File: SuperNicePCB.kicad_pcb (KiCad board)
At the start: 4 copper layers, 75 x 85 mm, 65 parts, among them J1 UART Debug, J2 Boot Opt, SW1 Reset, U1 ESP32-S3-WROOM-1-N8, U2 SY8089AAAC, U3 SGM2048-ADJXTEK8G/TR, U4 ICS-43434_C5656610, U5 AM312, U6 SCD40-D-R1, U7 SHT40-AD1B-R3, U8 HLK-LD6002, U9 DWM3000TR13

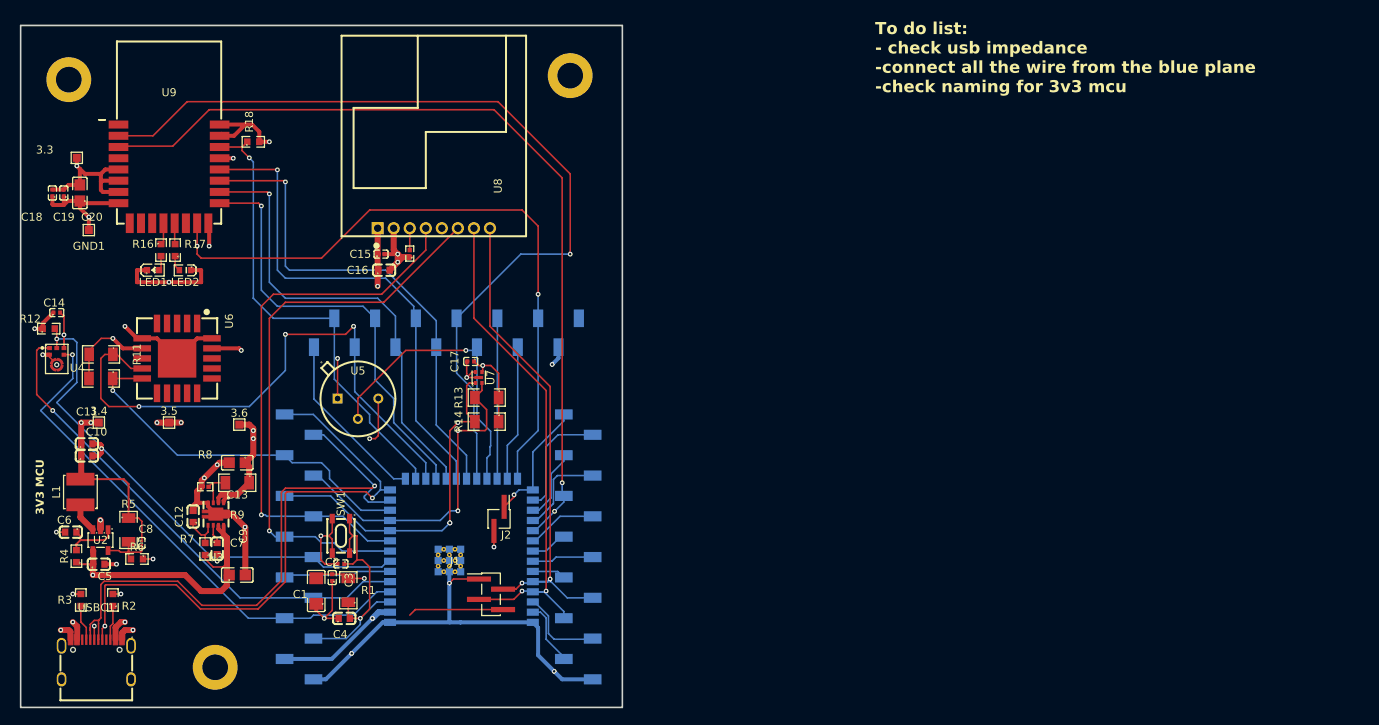
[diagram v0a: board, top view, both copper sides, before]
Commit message: Connect power for uart debug
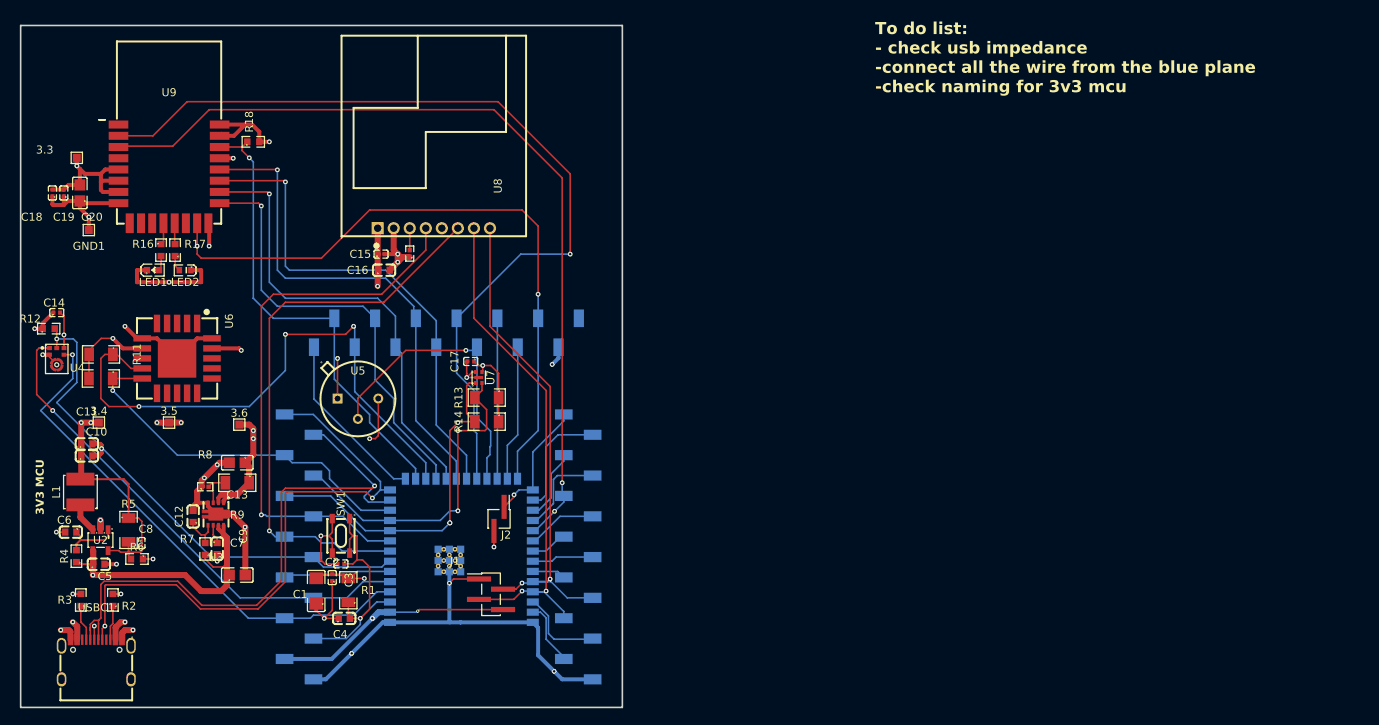
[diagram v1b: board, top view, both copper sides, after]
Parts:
- removed REF** (x3): MountingHole_3.2mm_M3_DIN965_Pad, MountingHole:MountingHole_3.2mm_M3_DIN965_Pad
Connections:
- J1 pad 4: /MCU/VDD33 -> /MCU/3V3_MCU
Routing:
- net /MCU/3V3_MCU: track 115.4 -> 129.7 mm, vias 4 -> 5
- net /MCU/VDD33: track 11.9 -> 0.00 mm

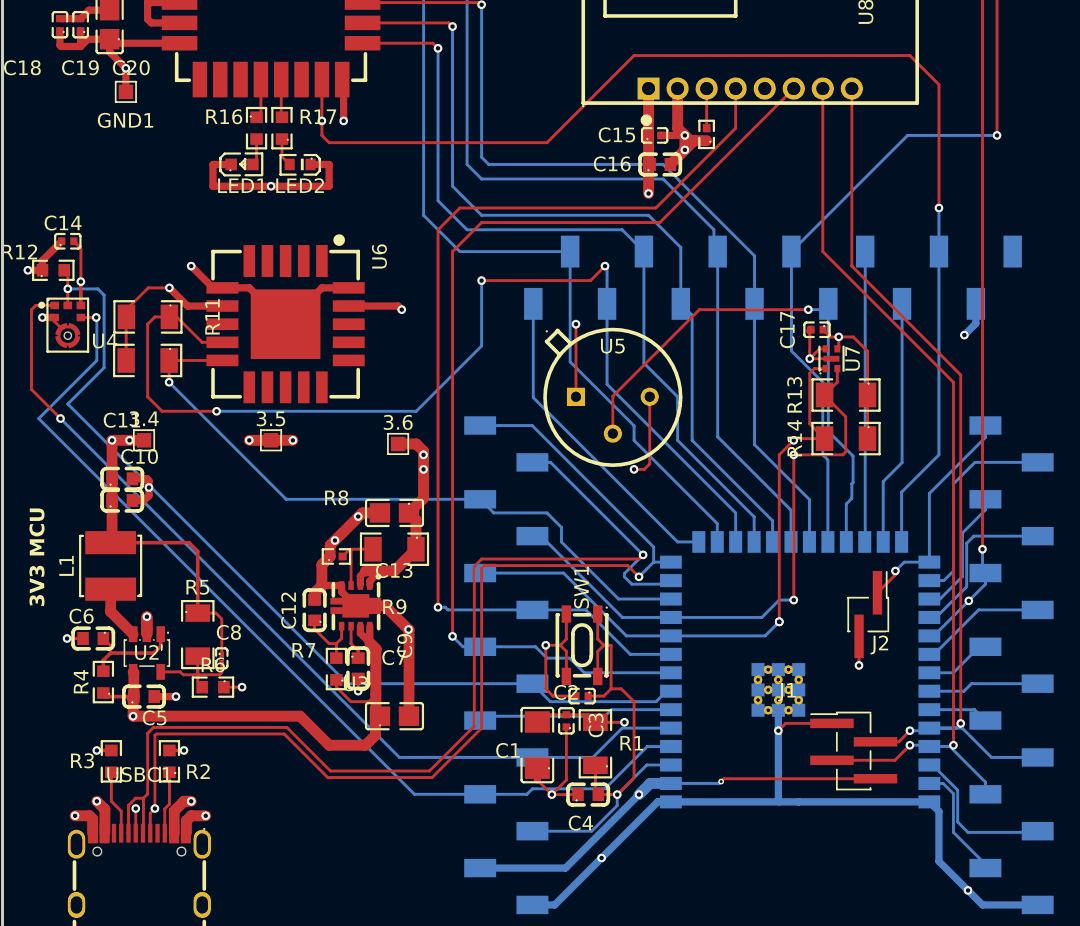
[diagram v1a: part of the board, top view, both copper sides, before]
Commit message: DRC issues resolved
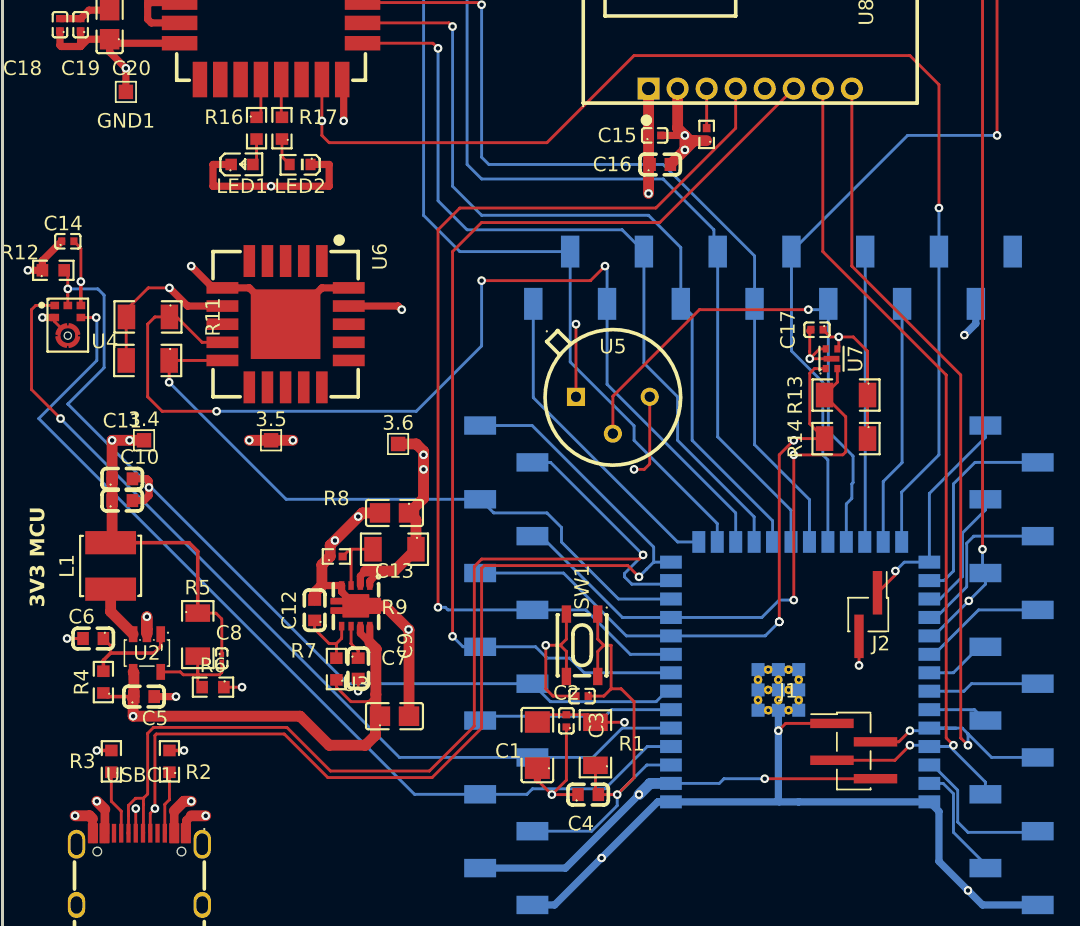
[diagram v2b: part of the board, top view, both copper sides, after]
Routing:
- net /MCU/RXD: track 61.5 -> 63.6 mm
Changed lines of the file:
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@@
 		(at 138.6 110.38 90)
 		(property "Reference" "U7"
-			(at 0 1.48 90)
+			(at 0 1.65 90)
 			(layer "F.SilkS")
 			(effects
@@
 		(at 151 131.49 90)
 		(property "Reference" "H3"
-			(at 0.65 3 90)
+			(at 0.99 2.5 90)
 			(layer "B.SilkS")
 			(effects
@@
 	)
 	(segment
-		(start 131.195 139.305)
-		(end 131 139.5)
-		(width 0.2)
-		(layer "F.Cu")
-		(net "/MCU/3V3_MCU")
-	)
-	(segment
 		(start 89.05 118.65)
 		(end 89.05 122.95)
@@
 	)
 	(segment
-		(start 141.63 139.305)
-		(end 131.195 139.305)
-		(width 0.2)
-		(layer "F.Cu")
-		(net "/MCU/3V3_MCU")
-	)
-	(segment
 		(start 88.95 123.05)
 		(end 94.35 123.05)
@@
 	)
 	(segment
+		(start 134 139.305)
+		(end 141.63 139.305)
+		(width 0.2)
+		(layer "F.Cu")
+		(net "/MCU/3V3_MCU")
+	)
+	(segment
 		(start 96.2 127.9)
 		(end 96.604808 128.304808)
@@
 	)
 	(via
-		(at 131 139.5)
-		(size 0.4)
-		(drill 0.2)
+		(at 134 139.305)
+		(size 0.6)
+		(drill 0.3)
 		(layers "F.Cu" "B.Cu")
 		(net "/MCU/3V3_MCU")
@@
 	)
 	(segment
-		(start 127.54 139.63)
-		(end 130.87 139.63)
-		(width 0.2)
-		(layer "B.Cu")
-		(net "/MCU/3V3_MCU")
-	)
-	(segment
-		(start 130.87 139.63)
-		(end 131 139.5)
-		(width 0.2)
-		(layer "B.Cu")
-		(net "/MCU/3V3_MCU")
-	)
-	(segment
 		(start 125.34 140.4)
 		(end 120.28 145.46)
@@
 	)
 	(segment
+		(start 134 139.305)
+		(end 131.195 139.305)
+		(width 0.2)
+		(layer "B.Cu")
+		(net "/MCU/3V3_MCU")
+	)
+	(segment
 		(start 126.11 139.63)
 		(end 125.34 140.4)
@@
 	)
 	(segment
+		(start 130.87 139.63)
+		(end 127.54 139.63)
+		(width 0.2)
+		(layer "B.Cu")
+		(net "/MCU/3V3_MCU")
+	)
+	(segment
+		(start 131.195 139.305)
+		(end 130.87 139.63)
+		(width 0.2)
+		(layer "B.Cu")
+		(net "/MCU/3V3_MCU")
+	)
+	(segment
 		(start 114 138)
 		(end 114 141.4)
@@
 		(start 87.705102 142.065014)
 		(end 87.705102 143.06)
-		(width 0.75)
+		(width 0.6)
 		(layer "F.Cu")
 		(net "GND")
@@
 	)
 	(segment
+		(start 94.17 142.189912)
+		(end 94.5 141.859912)
+		(width 0.6)
+		(layer "F.Cu")
+		(net "GND")
+	)
+	(segment
 		(start 119.42 133.615)
 		(end 121 133.615)
@@
 	)
 	(segment
-		(start 94.5 141.859912)
-		(end 94.17 142.189912)
-		(width 0.75)
-		(layer "F.Cu")
-		(net "GND")
-	)
-	(segment
 		(start 96.65 105.5)
 		(end 98.5 105.5)
@@
 	)
 	(segment
-		(start 87.5 141.859912)
-		(end 87.705102 142.065014)
-		(width 0.75)
-		(layer "F.Cu")
-		(net "GND")
-	)
-	(segment
 		(start 84.25 103.62)
 		(end 85.58 102.29)
@@
 	)
 	(segment
+		(start 87.5 141.859912)
+		(end 87.705102 142.065014)
+		(width 0.75)
+		(layer "F.Cu")
+		(net "GND")
+	)
+	(segment
 		(start 103 127)
 		(end 103 126.5)
@@
 		(start 94.17 142.189912)
 		(end 94.17 143.06)
-		(width 0.75)
+		(width 0.6)
 		(layer "F.Cu")
 		(net "GND")
@@
 	)
 	(segment
-		(start 140 91.7725)
+		(start 147.5 111.5)
 		(end 140 104)
 		(width 0.2)
@@
 	)
 	(segment
-		(start 147.5 111.5)
-		(end 147.5 135.5)
+		(start 143.235 136.765)
+		(end 144 136)
 		(width 0.2)
 		(layer "F.Cu")
@@
 	)
 	(segment
-		(start 143.235 136.765)
-		(end 144 136)
+		(start 140 104)
+		(end 140 91.7725)
 		(width 0.2)
 		(layer "F.Cu")
@@
 	)
 	(segment
-		(start 140 104)
+		(start 148 137)
+		(end 147.5 136.5)
+		(width 0.2)
+		(layer "F.Cu")
+		(net "/MCU/RXD")
+	)
+	(segment
+		(start 147.5 136.5)
 		(end 147.5 111.5)
 		(width 0.2)
@@
 	)
 	(via
-		(at 147.5 135.5)
+		(at 148 137)
 		(size 0.6)
 		(drill 0.3)
@@
 	)
 	(segment
-		(start 147.605 135.82)
+		(start 148.0175 136.2325)
 		(end 149.625 137.84)
 		(width 0.2)
@@
 	)
 	(segment
+		(start 148 137)
+		(end 148 136.25)
+		(width 0.2)
+		(layer "B.Cu")
+		(net "/MCU/RXD")
+	)
+	(segment
 		(start 144 136)
 		(end 145.16 136)
@@
 	)
 	(segment
-		(start 145.34 135.82)
-		(end 147.18 135.82)
+		(start 148 136.25)
+		(end 148.0175 136.2325)
 		(width 0.2)
 		(layer "B.Cu")
@@
 	(segment
 		(start 147.18 135.82)
-		(end 147.5 135.5)
+		(end 145.34 135.82)
+		(width 0.2)
+		(layer "B.Cu")
+		(net "/MCU/RXD")
+	)
+	(segment
+		(start 147.605 135.82)
+		(end 148.0175 136.2325)
 		(width 0.2)
 		(layer "B.Cu")
@@
 	(segment
 		(start 138 103)
-		(end 147 112)
+		(end 146.5 111.5)
 		(width 0.2)
 		(layer "F.Cu")
@@
 	)
 	(segment
-		(start 147 112)
+		(start 146.5 136.5)
 		(end 147 137)
 		(width 0.2)
@@
 	)
 	(segment
-		(start 138.63 138.035)
-		(end 142.965 138.035)
+		(start 146.5 111.5)
+		(end 146.5 136.5)
 		(width 0.2)
 		(layer "F.Cu")
@@
 	)
 	(segment
-		(start 142.965 138.035)
-		(end 144 137)
+		(start 138 91.7725)
+		(end 138 103)
 		(width 0.2)
 		(layer "F.Cu")
@@
 	)
 	(segment
-		(start 138 91.7725)
-		(end 138 103)
+		(start 138.63 138.035)
+		(end 142.965 138.035)
+		(width 0.2)
+		(layer "F.Cu")
+		(net "/MCU/TXD")
+	)
+	(segment
+		(start 142.965 138.035)
+		(end 144 137)
 		(width 0.2)
 		(layer "F.Cu")
@@
 	)
 	(segment
-		(start 93 141.060882)
-		(end 92.68 141.380882)
+		(start 93 138.859912)
+		(end 93 140.75)
 		(width 0.2)
 		(layer "F.Cu")
@@
 	)
 	(segment
-		(start 93 138.859912)
-		(end 93 141.060882)
+		(start 92.68 141.07)
+		(end 92.68 143.06)
 		(width 0.2)
 		(layer "F.Cu")
@@
 	)
 	(segment
-		(start 92.68 141.380882)
-		(end 92.68 143.06)
+		(start 93 140.75)
+		(end 92.68 141.07)
 		(width 0.2)
 		(layer "F.Cu")
@@
 		(start 93.33 141.529912)
 		(end 93.33 143.06)
-		(width 0.75)
+		(width 0.6)
 		(layer "F.Cu")
 		(net "Net-(U2-IN)")
@@
 		(start 88.554923 141.414835)
 		(end 88.554923 143.06)
-		(width 0.75)
+		(width 0.6)
 		(layer "F.Cu")
 		(net "Net-(U2-IN)")
@@
 	)
 	(segment
-		(start 90.18 141.859912)
-		(end 90.18 143.06)
-		(width 0.2)
-		(layer "F.Cu")
-		(net "/USB_D-")
-	)
-	(segment
 		(start 101.093198 135.775)
 		(end 104.093198 138.775)
@@
 	)
 	(segment
+		(start 90.18 141.859912)
+		(end 90.18 143.06)
+		(width 0.2)
+		(layer "F.Cu")
+		(net "/USB_D-")
+	)
+	(segment
 		(start 114.506802 124.175)
 		(end 125.355 124.175)
@@
 	)
 	(segment
-		(start 90.176 141.855912)
-		(end 90.18 141.859912)
-		(width 0.2)
-		(layer "F.Cu")
-		(net "/USB_D-")
-	)
-	(segment
 		(start 90.151 143.031)
 		(end 90.18 143.06)
@@
 		(width 0.2)
 		(layer "F.Cu")
+		(net "/USB_D-")
+	)
+	(segment
+		(start 90.176 141.855912)
+		(end 90.18 141.859912)
+		(width 0.2)
+		(layer "F.Cu")

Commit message: Naming shit
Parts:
- renumbered 3.4 to 3V3_M, 3.6 to 3V3_S, 3.3 to 3V3_S, 3.5 to GND, GND1 to GND
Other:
- board text removed: "3V3 MCU"

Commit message: Bit of cleanup/ checked usb lenght
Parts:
- moved USBC1 1.00 mm to (90.9, 146.5)
- moved C10 0.41 mm to (89.8, 120.6)
- renumbered 3V3_S to 3.3, GND to GND1
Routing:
- net GND: track 250.3 -> 230.5 mm
- net /USB_D-: track 74.5 -> 76.8 mm
- net Net-(U2-IN): track 56.8 -> 58.8 mm
- net /USB_D+: track 76.4 -> 78.4 mm
- net /TEMP_SCL: track 41.5 -> 40.3 mm, vias 2 -> 1
- net Net-(USBC1-CC2): track 4.33 -> 5.33 mm
- net Net-(USBC1-CC1): track 4.48 -> 5.48 mm
- net /TEMP_SDA: vias 3 -> 1
- net /MCU/UWB_RXOK: vias 2 -> 1
- net /MCU/UWB_RST: vias 2 -> 1
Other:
- board text removed: "To do list: - check usb impedance -connect all the wire from the blue plane -check naming for 3v3 mcu"

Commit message: Various Cleanup and shit
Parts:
- added REF**: MountingHole_2.2mm_M2_ISO14580_Pad_TopBottom, MountingHole:MountingHole_2.2mm_M2_ISO14580_Pad_TopBottom, F.Cu at (87.0, 72.0)
- added REF**: MountingHole_2.2mm_M2_ISO14580_Pad_TopBottom, MountingHole:MountingHole_2.2mm_M2_ISO14580_Pad_TopBottom, F.Cu at (152.0, 110.0)
- added REF**: MountingHole_2.2mm_M2_ISO14580_Pad_TopBottom, MountingHole:MountingHole_2.2mm_M2_ISO14580_Pad_TopBottom, F.Cu at (151.0, 71.0)
- added REF**: MountingHole_2.2mm_M2_ISO14580_Pad_TopBottom, MountingHole:MountingHole_2.2mm_M2_ISO14580_Pad_TopBottom, F.Cu at (103.0, 147.0)
- UART : renamed from J1
- renumbered J2 to BOOT, GND1 to GND, SW1 to RESET

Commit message: Label + test commit Mathieu
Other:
- board size 75 x 85 mm -> 76 x 85 mm
- board text added: "BOOT"
- board text added: "GND"
- board text added: "IO1"
- board text added: "IO2"
- board text added: "IO35"
- board text added: "IO36"
- board text added: "IO37"
- board text added: "IO39"
- board text added: "IO40"
- board text added: "IO41"
- board text added: "IO42"
- board text added: "RXD"
- board text added: "TXD"
- board text added: "UWB_RST"
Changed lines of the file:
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@@
 		(at 151 131.49 90)
 		(property "Reference" "H3"
-			(at 0.99 2.5 90)
+			(at 1.49 0 90)
 			(layer "B.SilkS")
 			(effects
@@
 	(gr_rect
 		(start 81.5 66.5)
-		(end 156.5 151.5)
+		(end 157.5 151.5)
 		(radius 2)
 		(stroke
@@
 		(layer "Edge.Cuts")
 	)
+	(gr_text "UWB_RST"
+		(at 152.5 125 180)
+		(layer "B.SilkS")
+		(effects
+			(font
+				(size 0.7 0.7)
+				(thickness 0.1)
+			)
+			(justify left bottom mirror)
+		)
+	)
+	(gr_text "BOOT"
+		(at 154.5 114.5 180)
+		(layer "B.SilkS")
+		(effects
+			(font
+				(size 0.7 0.7)
+				(thickness 0.1)
+			)
+			(justify left bottom mirror)
+		)
+	)
+	(gr_text "IO35"
+		(at 154.5 117 180)
+		(layer "B.SilkS")
+		(effects
+			(font
+				(size 0.7 0.7)
+				(thickness 0.1)
+			)
+			(justify left bottom mirror)
+		)
+	)
+	(gr_text "IO36"
+		(at 154.5 120 180)
+		(layer "B.SilkS")
+		(effects
+			(font
+				(size 0.7 0.7)
+				(thickness 0.1)
+			)
+			(justify left bottom mirror)
+		)
+	)
+	(gr_text "IO37"
+		(at 154.5 122.5 180)
+		(layer "B.SilkS")
+		(effects
+			(font
+				(size 0.7 0.7)
+				(thickness 0.1)
+			)
+			(justify left bottom mirror)
+		)
+	)
+	(gr_text "IO39"
+		(at 154.5 127.5 180)
+		(layer "B.SilkS")
+		(effects
+			(font
+				(size 0.7 0.7)
+				(thickness 0.1)
+			)
+			(justify left bottom mirror)
+		)
+	)
+	(gr_text "IO40"
+		(at 154.5 130 180)
+		(layer "B.SilkS")
+		(effects
+			(font
+				(size 0.7 0.7)
+				(thickness 0.1)
+			)
+			(justify left bottom mirror)
+		)
+	)
+	(gr_text "IO41"
+		(at 154.5 132.5 180)
+		(layer "B.SilkS")
+		(effects
+			(font
+				(size 0.7 0.7)
+				(thickness 0.1)
+			)
+			(justify left bottom mirror)
+		)
+	)
+	(gr_text "IO42"
+		(at 154.5 135 180)
+		(layer "B.SilkS")
+		(effects
+			(font
+				(size 0.7 0.7)
+				(thickness 0.1)
+			)
+			(justify left bottom mirror)
+		)
+	)
+	(gr_text "RXD"
+		(at 154.5 137.5 180)
+		(layer "B.SilkS")
+		(effects
+			(font
+				(size 0.7 0.7)
+				(thickness 0.1)
+			)
+			(justify left bottom mirror)
+		)
+	)
+	(gr_text "TXD"
+		(at 154.5 140 180)
+		(layer "B.SilkS")
+		(effects
+			(font
+				(size 0.7 0.7)
+				(thickness 0.1)
+			)
+			(justify left bottom mirror)
+		)
+	)
+	(gr_text "IO2"
+		(at 154.5 142.5 180)
+		(layer "B.SilkS")
+		(effects
+			(font
+				(size 0.7 0.7)
+				(thickness 0.1)
+			)
+			(justify left bottom mirror)
+		)
+	)
+	(gr_text "IO1"
+		(at 154.5 145 180)
+		(layer "B.SilkS")
+		(effects
+			(font
+				(size 0.7 0.7)
+				(thickness 0.1)
+			)
+			(justify left bottom mirror)
+		)
+	)
+	(gr_text "GND"
+		(at 154.5 147.5 180)
+		(layer "B.SilkS")
+		(effects
+			(font
+				(size 0.7 0.7)
+				(thickness 0.1)
+			)
+			(justify left bottom mirror)
+		)
+	)
 	(dimension

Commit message: Labels
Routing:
- net /MCU/UWB_WAKEUP: track 110.3 -> 111.7 mm
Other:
- board text added: "3V3_MCU"
- board text added: "AC_BCLK"
- board text added: "AC_DOUT"
- board text added: "AC_LRCLK"
- board text added: "C02_SDA"
- board text added: "CO2_SCL"
- board text added: "DIN"
- board text added: "EN"
- board text added: "IO3"
- board text added: "IO47"
- board text added: "IO48"
- board text added: "PIR_OUT"
- board text added: "TEMP_SCL"
- board text added: "TEMP_SDA"
- board text added: "U0_CTS"
- board text added: "U0_RTS"
- board text added: "USB_D+"
- board text added: "USB_D-"
- board text added: "UWB_CS0"
- board text added: "UWB_IRQ"
- board text added: "UWB_MISO"
- board text added: "UWB_MOSI"
- board text added: "UWB_RXOK"
- board text added: "UWB_SCK"
- board text added: "UWB_WAKEUP"
- board text added: "X"

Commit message: Named shit
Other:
- board text added: "ECAM Engeneering"
- board text added: "M.V.L.L"
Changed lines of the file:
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@@
 		(layer "Edge.Cuts")
+	)
+	(gr_text "ECAM Engeneering"
+		(at 101.5 150.75 0)
+		(layer "F.SilkS")
+		(effects
+			(font
+				(size 1 1)
+				(thickness 0.1)
+				(italic yes)
+			)
+			(justify left bottom)
+		)
+	)
+	(gr_text "M.V.L.L"
+		(at 106 148.25 0)
+		(layer "F.SilkS")
+		(effects
+			(font
+				(size 1.5 1.5)
+				(thickness 0.3)
+				(bold yes)
+			)
+			(justify left bottom)
+		)
 	)
 	(gr_text "TEMP_SDA"
@@
 		)
 	)
-	(dimension
-		(type orthogonal)
-		(layer "In2.Cu")
-		(pts
-			(xy 73 50) (xy 173 50)
-		)
-		(height -2)
-		(orientation 0)
-		(format
-			(prefix "")
-			(suffix "")
-			(units 3)
-			(units_format 0)
-			(precision 4)
-			(suppress_zeroes yes)
-		)
-		(style
-			(thickness 0.2)
-			(arrow_length 1.27)
-			(text_position_mode 0)
-			(arrow_direction outward)
-			(extension_height 0.58642)
-			(extension_offset 0.5)
-			(keep_text_aligned yes)
-		)
-		(gr_text "100"
-			(at 123 46.2 0)
-			(layer "In2.Cu")
-			(effects
-				(font
-					(size 1.5 1.5)
-					(thickness 0.3)
-				)
-			)
-		)
-	)
-	(dimension
-		(type orthogonal)
-		(layer "In2.Cu")
-		(pts
-			(xy 73 50) (xy 73 150)
-		)
-		(height -7)
-		(orientation 1)
-		(format
-			(prefix "")
-			(suffix "")
-			(units 3)
-			(units_format 0)
-			(precision 4)
-			(suppress_zeroes yes)
-		)
-		(style
-			(thickness 0.2)
-			(arrow_length 1.27)
-			(text_position_mode 0)
-			(arrow_direction outward)
-			(extension_height 0.58642)
-			(extension_offset 0.5)
-			(keep_text_aligned yes)
-		)
-		(gr_text "100"
-			(at 64.2 100 90)
-			(layer "In2.Cu")
-			(effects
-				(font
-					(size 1.5 1.5)
-					(thickness 0.3)
-				)
-			)
-		)
-	)
